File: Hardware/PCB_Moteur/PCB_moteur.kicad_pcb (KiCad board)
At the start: 2 copper layers, 191 parts, among them J1 XT30PW-F, J10 Conn_01x02, J11 Conn_01x02, J12 Conn_01x02, J13 Conn_01x02, J14 Conn_01x02, J15 Conn_01x02, J16 Conn_01x06_Pin, J17 Screw_Terminal_01x04, J18 Screw_Terminal_01x04, J19 Screw_Terminal_01x04, J2 Conn_01x06_Pin, J3 Conn_01x03_Socket, J4 Conn_01x03_Socket, J5 Conn_01x03_Socket, J6 Conn_01x03_Socket, J7 Conn_01x02, J8 Conn_01x02, J9 Conn_01x02, Q1 SI5442DU-T1-GE3, Q2 SI5442DU-T1-GE3, Q3 MMBT3904, Q4 SI7617DN-T1-GE3, U1 L6981N33DR, U2 STM32F103CBT6, U3 MCP1802T-5002I/OT, U4 LSF0204PWR, U5 ISOW1044, U6 LM393, U7 INA125UA/2K5, U8 INA125UA/2K5, U9 MAX6612MXK

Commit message: board size et exploration
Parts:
- moved R2 86.6 mm to (92.5, 60.0)
- moved R1 81.6 mm to (92.8, 66.0)
- moved H2 75.3 mm to (137.0, 39.5)
- moved J1 68.2 mm to (101.5, 43.0)
- moved C4 67.2 mm to (93.5, 73.0)
- moved F1 63.8 mm to (104.0, 57.0), turned to 90 degrees
- moved C1 60.7 mm to (94.5, 84.5)
- moved H1 56.7 mm to (89.0, 39.5)
- moved C10 55.0 mm to (204.0, 83.0)
- moved C11 55.0 mm to (204.0, 87.2)
- moved C12 55.0 mm to (204.0, 91.5)
- moved C13 55.0 mm to (204.0, 95.7)
- moved C14 55.0 mm to (213.5, 94.4)
- moved C15 55.0 mm to (161.7, 103.7)
- moved C16 55.0 mm to (161.7, 106.7)
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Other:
- board outline added: 60 x 120 mm

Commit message: début alim
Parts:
- C1: footprint Capacitor_SMD:C_0805_2012Metric -> Capacitor_THT:CP_Radial_D6.3mm_P2.50mm
- U7, U8: footprint pcb_moteur:INA125UA_2K5-M -> pcb_moteur:D16-L
- moved C10 151.3 mm to (55.5, 112.2)
- moved C11 151.3 mm to (55.5, 116.5)
- moved C12 151.3 mm to (55.5, 120.8)
- moved C13 151.3 mm to (55.5, 125.0)
- moved C14 151.3 mm to (65.0, 123.7)
- moved R3 151.3 mm to (68.4, 133.4)
- moved R4 151.3 mm to (68.4, 135.9)
- moved LED1 116.4 mm to (117.8, 26.5)
- moved R5 116.4 mm to (137.1, 24.3)
- moved L2 106.1 mm to (102.0, 109.5)
- moved C2 102.0 mm to (108.0, 71.5)
- moved C3 102.0 mm to (108.0, 74.5)
- moved C5 90.8 mm to (120.1, 113.0)
- moved C6 90.8 mm to (124.6, 100.9)
- moved C7 90.8 mm to (124.6, 103.9)
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
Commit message: Version avec vraiment les compo 3d
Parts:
- C1: footprint Capacitor_THT:CP_Radial_D6.3mm_P2.50mm -> Capacitor_SMD:C_0805_2012Metric
- U7, U8: footprint pcb_moteur:D16-L -> pcb_moteur:INA125UA_2K5-M
- moved C10 151.3 mm to (204.0, 83.0)
- moved C11 151.3 mm to (204.0, 87.2)
- moved C12 151.3 mm to (204.0, 91.5)
- moved C13 151.3 mm to (204.0, 95.7)
- moved C14 151.3 mm to (213.5, 94.4)
- moved R3 151.3 mm to (216.9, 104.1)
- moved R4 151.3 mm to (216.9, 106.6)
- moved LED1 116.4 mm to (197.5, 111.3)
- moved R5 116.4 mm to (216.9, 109.1)
- moved L2 106.1 mm to (208.0, 105.0)
- moved C2 102.0 mm to (209.0, 85.4)
- moved C3 102.0 mm to (209.0, 88.4)
- moved C5 90.8 mm to (209.0, 94.4)
- moved C6 90.8 mm to (213.5, 82.4)
- moved C7 90.8 mm to (213.5, 85.4)
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
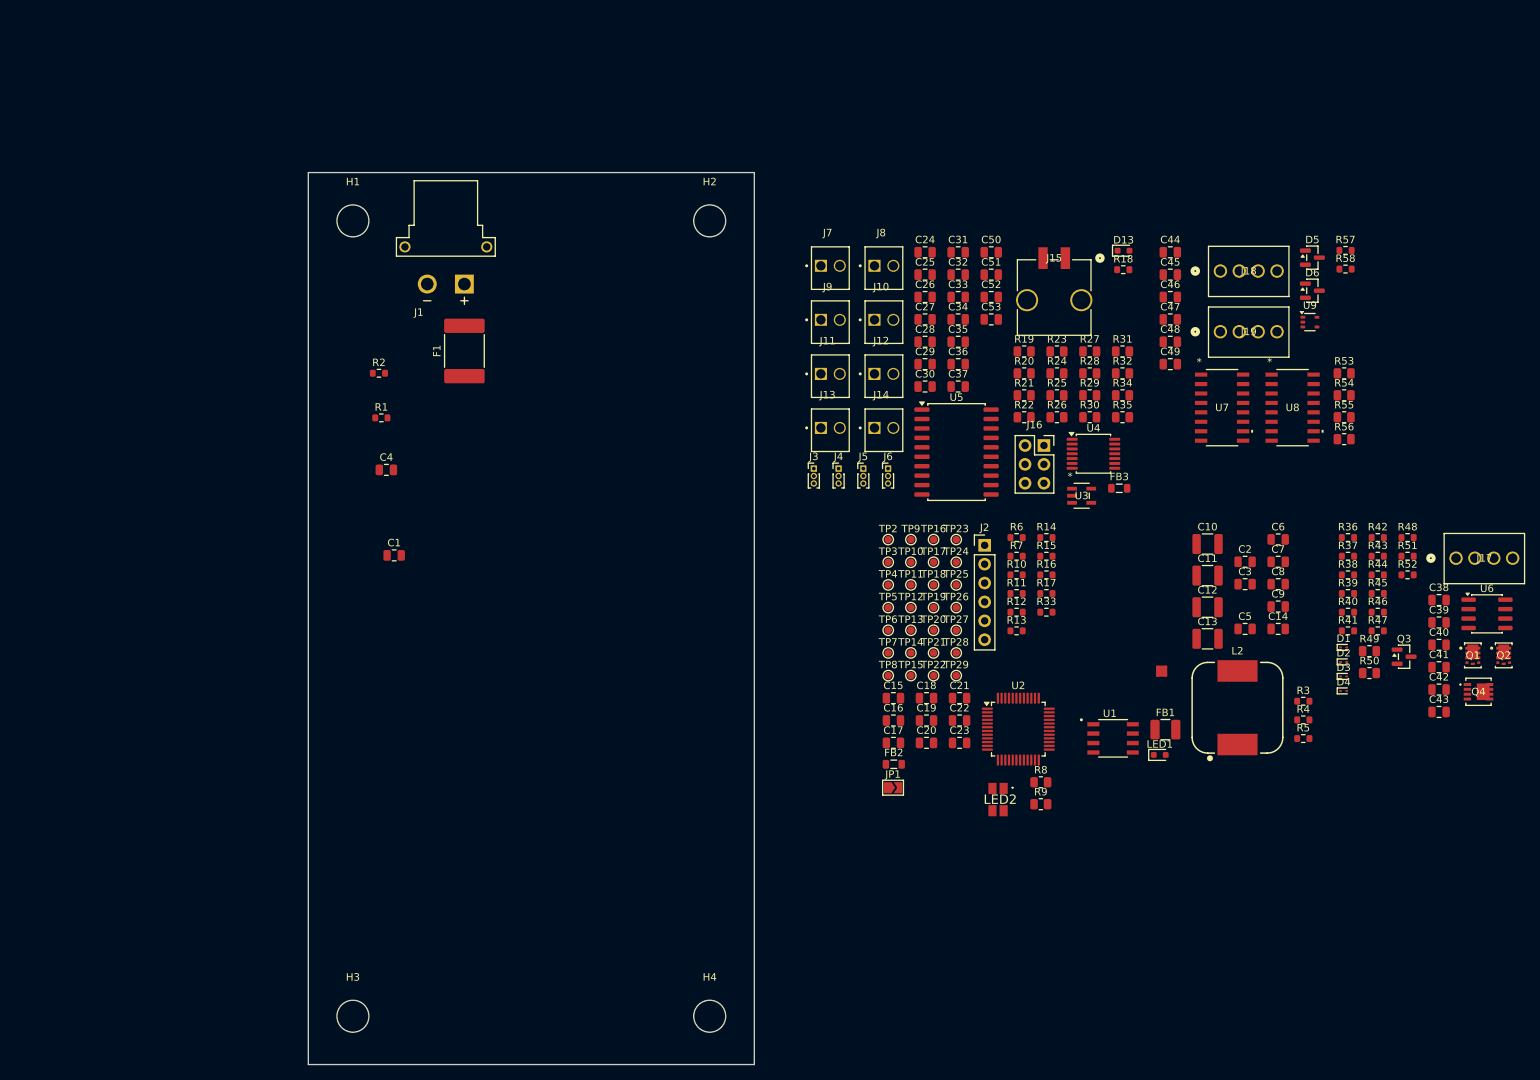
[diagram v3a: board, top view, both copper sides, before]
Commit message: Layout Alim 3.3V + pression et loadcell
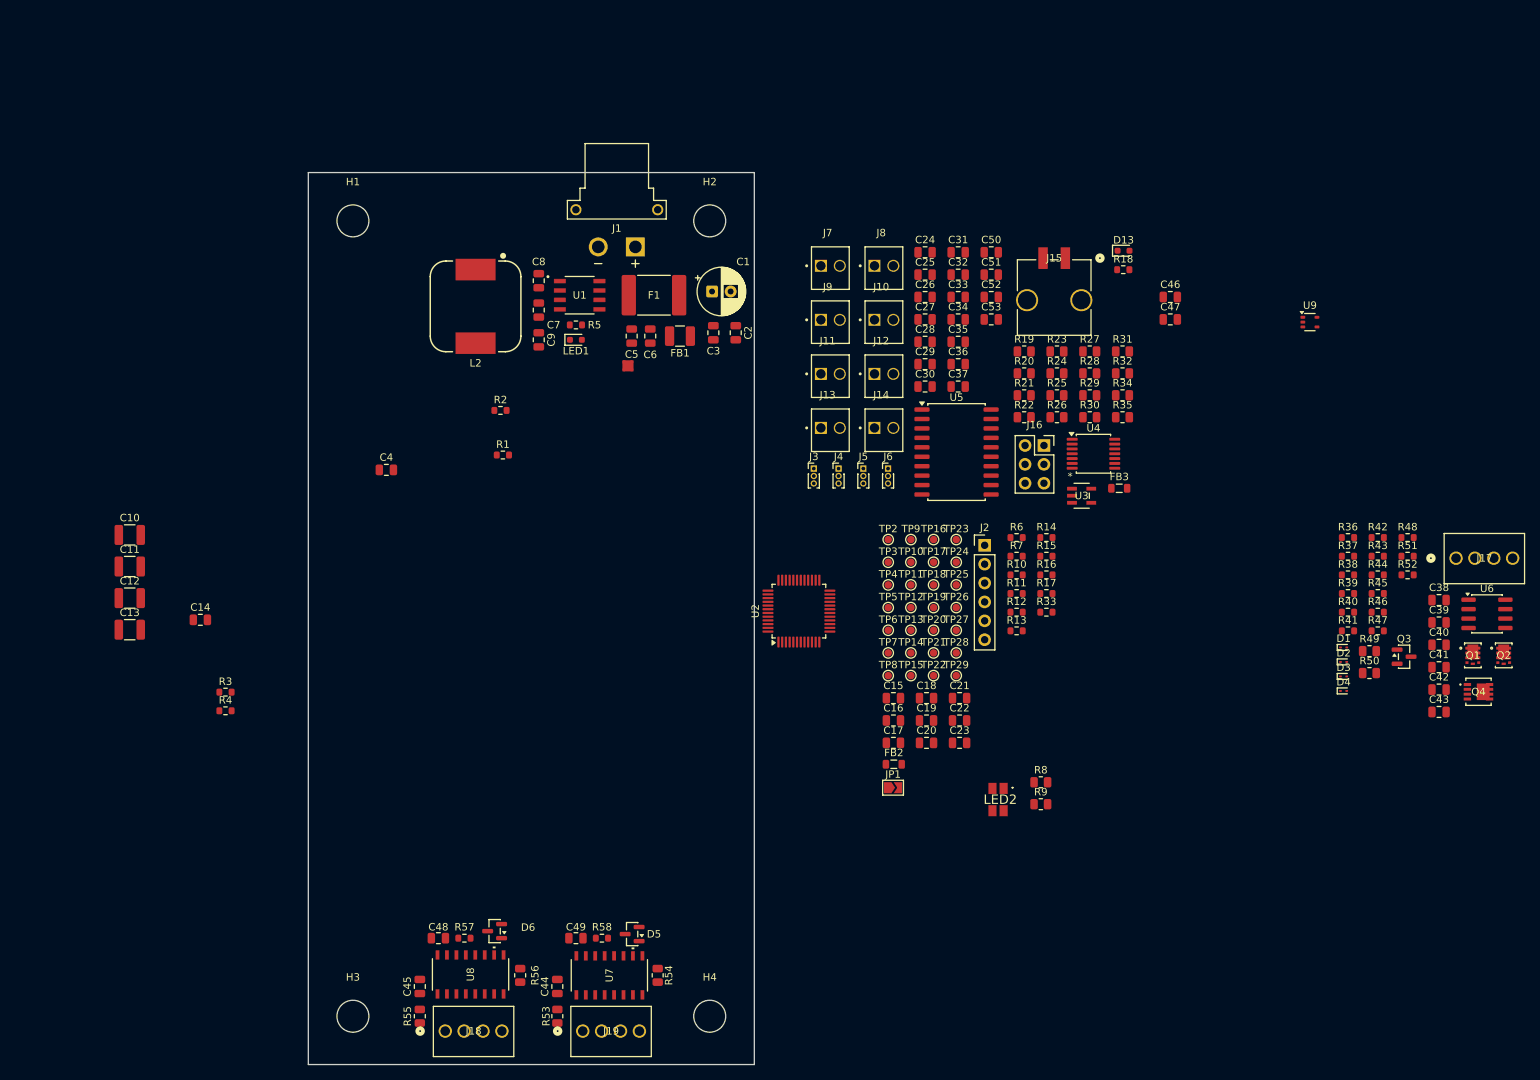
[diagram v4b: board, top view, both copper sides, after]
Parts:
- C1: footprint Capacitor_SMD:C_0805_2012Metric -> Capacitor_THT:CP_Radial_D6.3mm_P2.50mm
- U7, U8: footprint pcb_moteur:INA125UA_2K5-M -> pcb_moteur:D16-L
- moved R57 150.4 mm to (104.0, 136.0), turned to 180 degrees
- moved R55 148.2 mm to (98.0, 146.5), turned to 90 degrees
- moved J18 146.0 mm to (101.4, 148.5)
- moved C10 145.0 mm to (59.0, 81.8)
- moved C11 145.0 mm to (59.0, 86.0)
- moved C12 145.0 mm to (59.0, 90.2)
- moved C13 145.0 mm to (59.0, 94.5)
- moved C14 145.0 mm to (68.5, 93.2)
- moved R3 145.0 mm to (71.9, 102.9)
- moved R4 145.0 mm to (71.9, 105.4)
- moved D6 139.7 mm to (108.1, 135.1), turned to 180 degrees
- moved C45 139.2 mm to (98.0, 142.5), turned to 90 degrees
- moved R53 136.7 mm to (116.5, 146.5), turned to -90 degrees
- moved R58 134.6 mm to (122.5, 136.0), turned to 180 degrees
- moved U8 134.3 mm to (104.8, 140.9), turned to 90 degrees
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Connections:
- J18 pad 2: LC_OUT- -> LC_IN-
- J18 pad 4: LC_IN- -> LC_OUT-
- J19 pad 2: P_OUT- -> LC_IN-
- J19 pad 4: LC_IN- -> P_OUT-

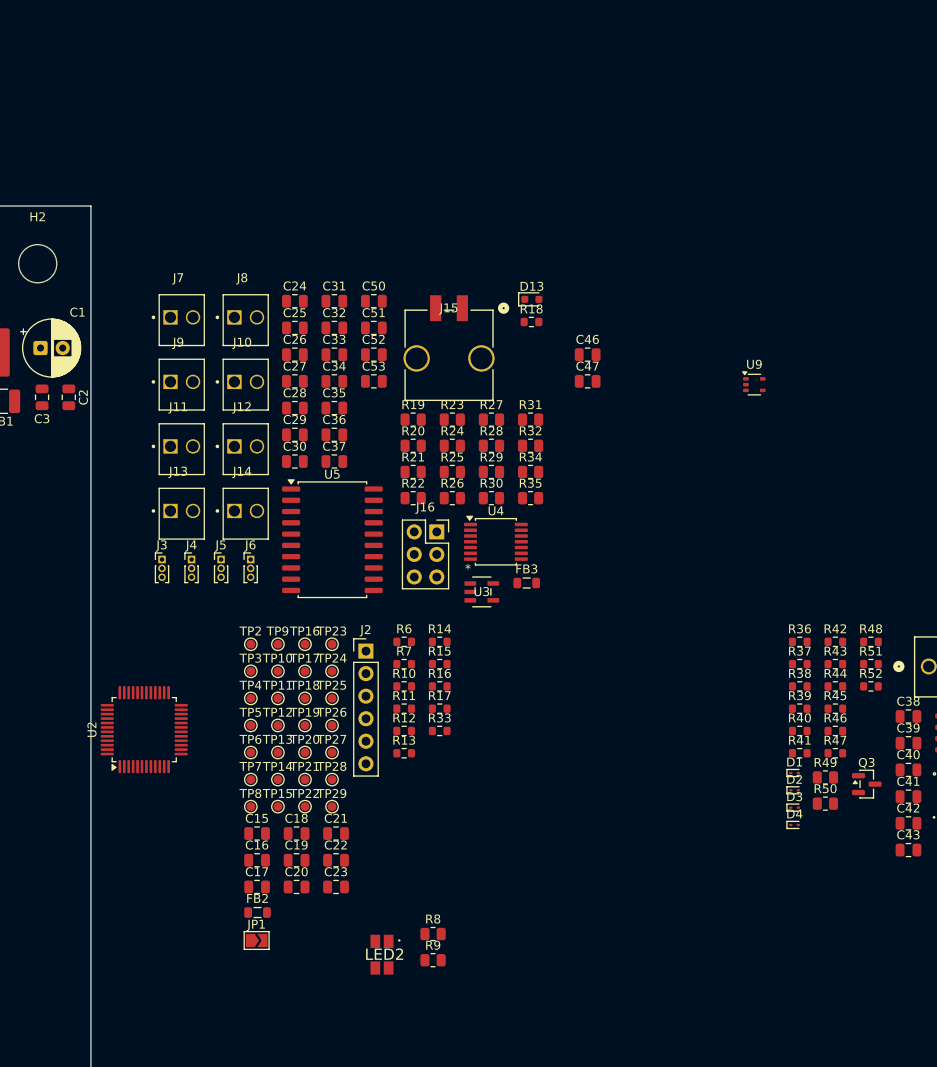
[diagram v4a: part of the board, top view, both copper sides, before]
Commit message: un peux de regroupement sans faire exactement le layout
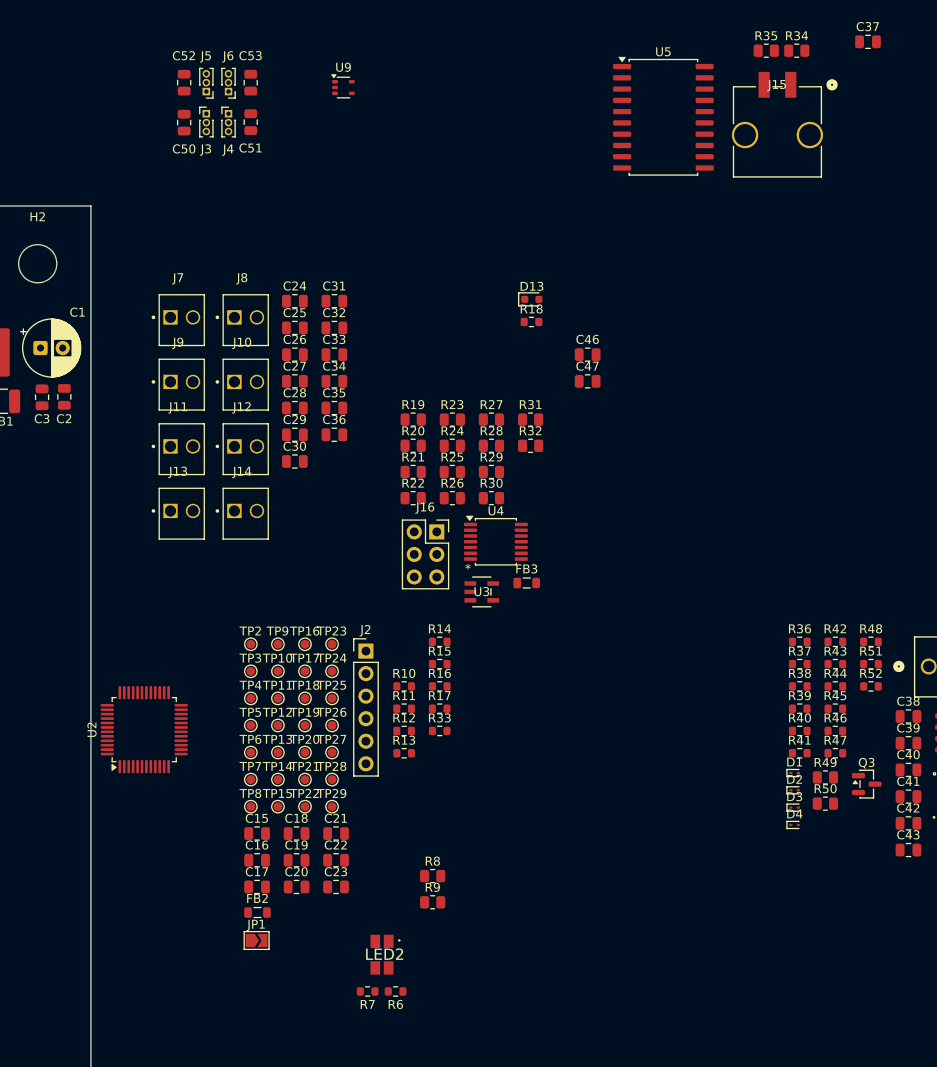
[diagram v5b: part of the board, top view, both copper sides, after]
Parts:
- moved C37 76.5 mm to (230.6, 14.5)
- moved U5 60.5 mm to (207.5, 23.0)
- moved U9 57.1 mm to (171.4, 19.6)
- moved R35 57.0 mm to (219.1, 15.5)
- moved R34 56.1 mm to (222.5, 15.5)
- moved J6 52.8 mm to (158.5, 20.1), turned to 180 degrees
- moved J5 52.8 mm to (156.0, 20.1), turned to 180 degrees
- moved J3 50.5 mm to (156.0, 22.6)
- moved J4 50.4 mm to (158.5, 22.6)
- moved J15 44.8 mm to (220.3, 24.6)
- moved R6 39.4 mm to (177.3, 121.5)
- moved C52 37.4 mm to (153.5, 19.1), turned to 90 degrees
- moved R7 37.1 mm to (174.2, 121.5)
- moved C53 36.4 mm to (161.0, 19.1), turned to 90 degrees
- moved C50 29.4 mm to (153.5, 23.6), turned to -90 degrees
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
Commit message: wip: layout circuits Pyro
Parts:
- R1, R10, R11, R12, R13, R14, R15, R16, R17, R18, R2, R3, R33, R36, R37, R38, R39, R4, R40, R41, R42, R43, R44, R45, R46, R47, R48, R5, R51, R52, R57, R58, R6, R7: footprint Resistor_SMD:R_0603_1608Metric -> Resistor_SMD:R_0805_2012Metric
- moved Q2 113.5 mm to (132.5, 76.0)
- moved C42 113.2 mm to (126.0, 72.5), turned to 90 degrees
- moved C38 112.4 mm to (123.0, 83.0), turned to -90 degrees
- moved U6 110.9 mm to (131.1, 82.5), turned to 90 degrees
- moved C40 110.2 mm to (125.0, 91.5), turned to -90 degrees
- moved Q4 109.6 mm to (137.0, 66.5), turned to -90 degrees
- moved Q1 107.5 mm to (132.5, 89.0)
- moved R47 105.7 mm to (123.5, 72.6), turned to -90 degrees
- moved D4 105.2 mm to (121.5, 72.5), turned to 90 degrees
- moved R44 101.4 mm to (126.0, 76.5)
- moved Q3 100.6 mm to (136.5, 61.9), turned to 90 degrees
- moved C43 100.5 mm to (140.0, 73.0), turned to 180 degrees
- moved R43 99.6 mm to (127.5, 91.6), turned to 90 degrees
- moved J17 99.6 mm to (138.0, 78.9), turned to -90 degrees
- moved R46 99.5 mm to (129.1, 73.5), turned to 180 degrees
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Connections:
- J17 pad 1: Vin_Pyro -> Pyro2-
- J17 pad 2: Pyro1- -> Vin_Pyro
- J17 pad 4: Pyro2- -> Pyro1-

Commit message: wip: début CAN Layout
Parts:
- moved C37 170.7 mm to (100.5, 125.0), turned to 90 degrees
- moved R34 167.5 mm to (98.0, 127.6), turned to -90 degrees
- moved J15 165.5 mm to (89.4, 125.8), turned to -90 degrees
- moved R35 162.6 mm to (98.0, 124.0), turned to -90 degrees
- moved U5 140.4 mm to (108.0, 122.0), turned to 180 degrees
- moved R12 20.5 mm to (113.5, 67.5)
- moved U2 8.86 mm to (108.5, 80.0)
